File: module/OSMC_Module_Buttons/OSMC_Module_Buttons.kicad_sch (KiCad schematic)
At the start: 4 parts, among them J1 Conn_01x08_Socket, U1 OSMC Module Board w/pins, U2 24LC02BT-I/OT, U3 PCF8574DWR

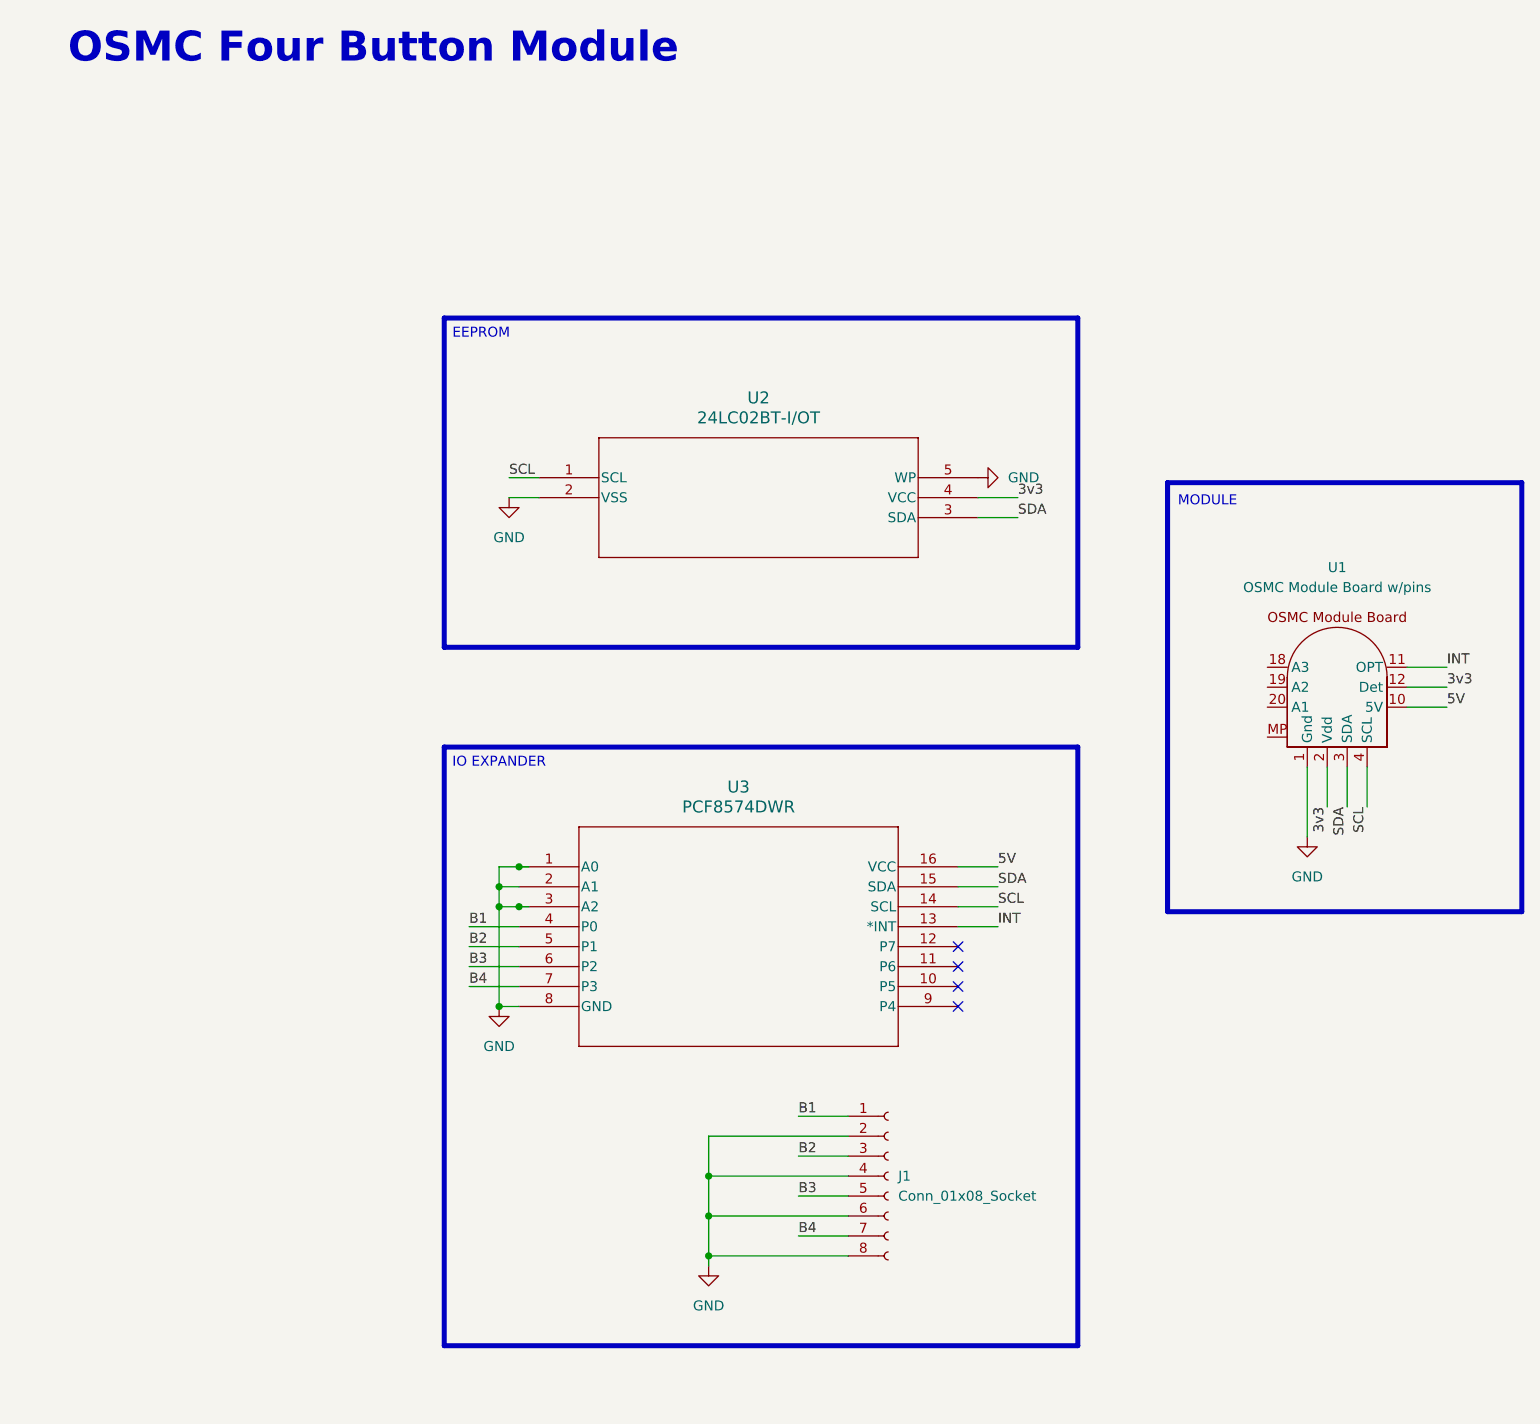
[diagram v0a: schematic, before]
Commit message: cleared via and traces
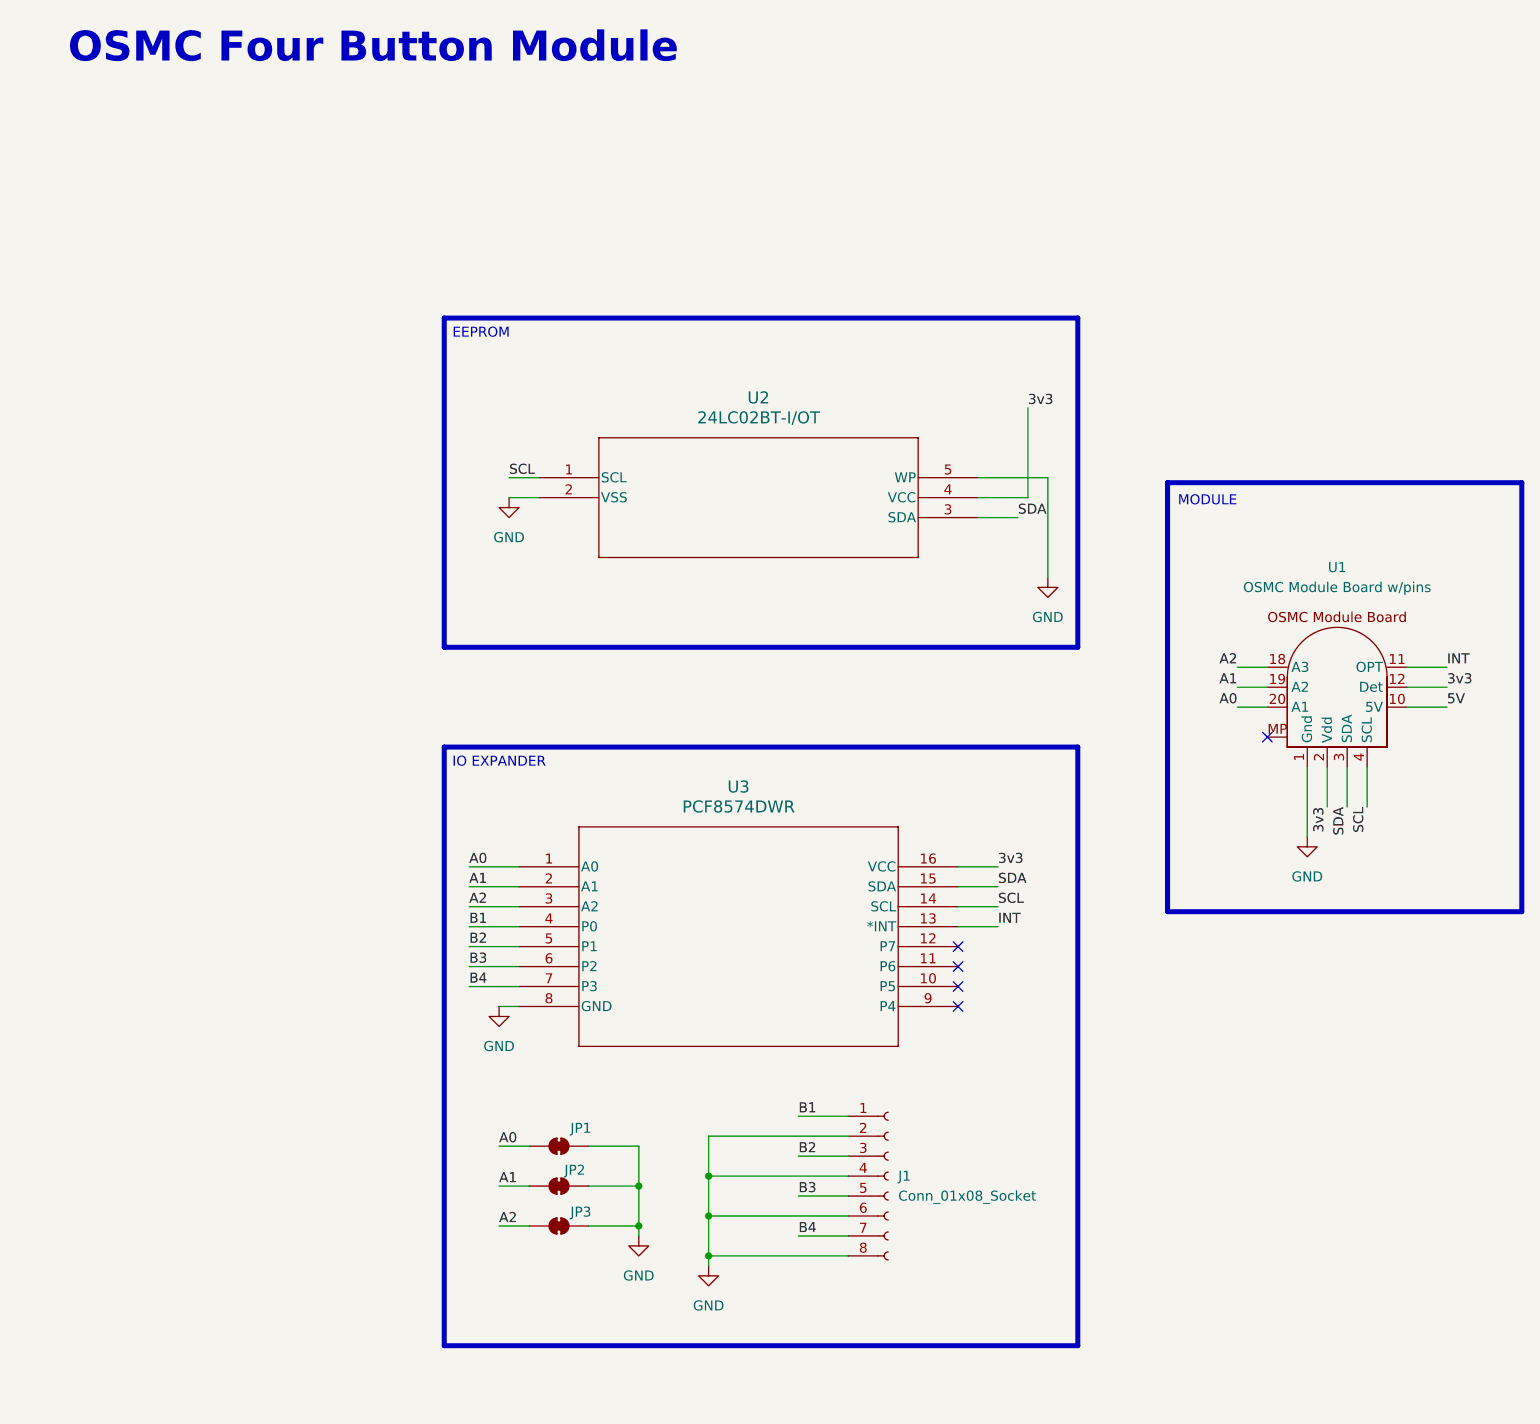
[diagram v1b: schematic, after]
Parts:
- added JP1, JP2, JP3: SolderJumper_2_Bridged, Jumper:SolderJumper-2_P1.3mm_Bridged2Bar_Pad1.0x1.5mm, symbol Jumper:SolderJumper_2_Bridged
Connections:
- net 3v3: now also U3.16 (VCC)
- net 5V: no longer U3.16 (VCC)
- net GND: now also JP1.2 (B), JP2.2 (B), JP3.2 (B); no longer U3.1 (A0), U3.2 (A1), U3.3 (A2)
- net A2: now reaches U1.18 (A3)
- net A2: now also U3.3 (A2), JP3.1 (A)
- net A1: now reaches U1.19 (A2)
- net A1: now also U3.2 (A1), JP2.1 (A)
- net A0: now reaches U1.20 (A1)
- net A0: now also U3.1 (A0), JP1.1 (A)
- no-connect marks 4 -> 5

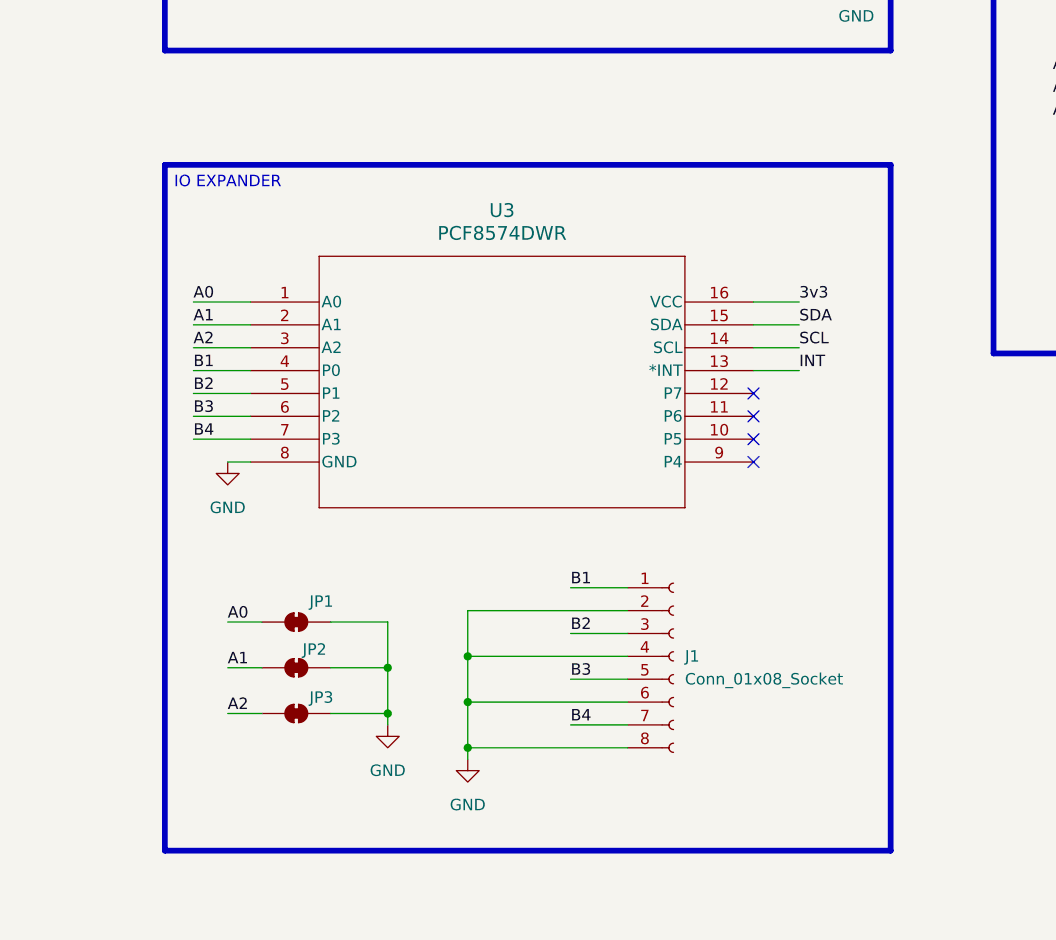
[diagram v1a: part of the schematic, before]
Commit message: update to modules gerbers produced
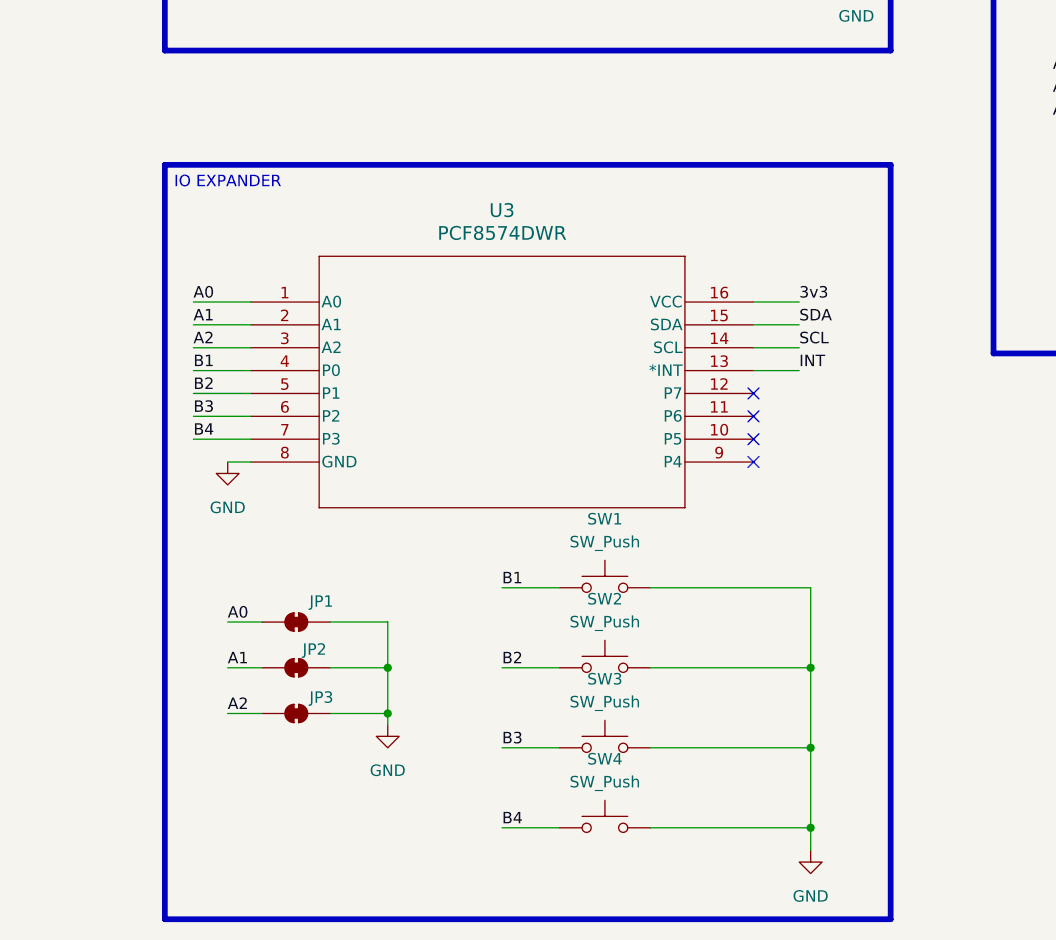
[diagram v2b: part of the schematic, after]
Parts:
- removed J1: Conn_01x08_Socket, Library:OSMC_Button_Membrane, symbol Library:Conn_01x08_Socket
- added SW1, SW2, SW3, SW4: SW_Push, footprints:SW_Push_1P1T_XKB_TS-1187A, symbol Switch:SW_Push
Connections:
- net B1: now also SW1.1
- net B2: now also SW2.1
- net B3: now also SW3.1
- net B4: now also SW4.1
- net GND: now also SW1.2, SW2.2, SW3.2, SW4.2

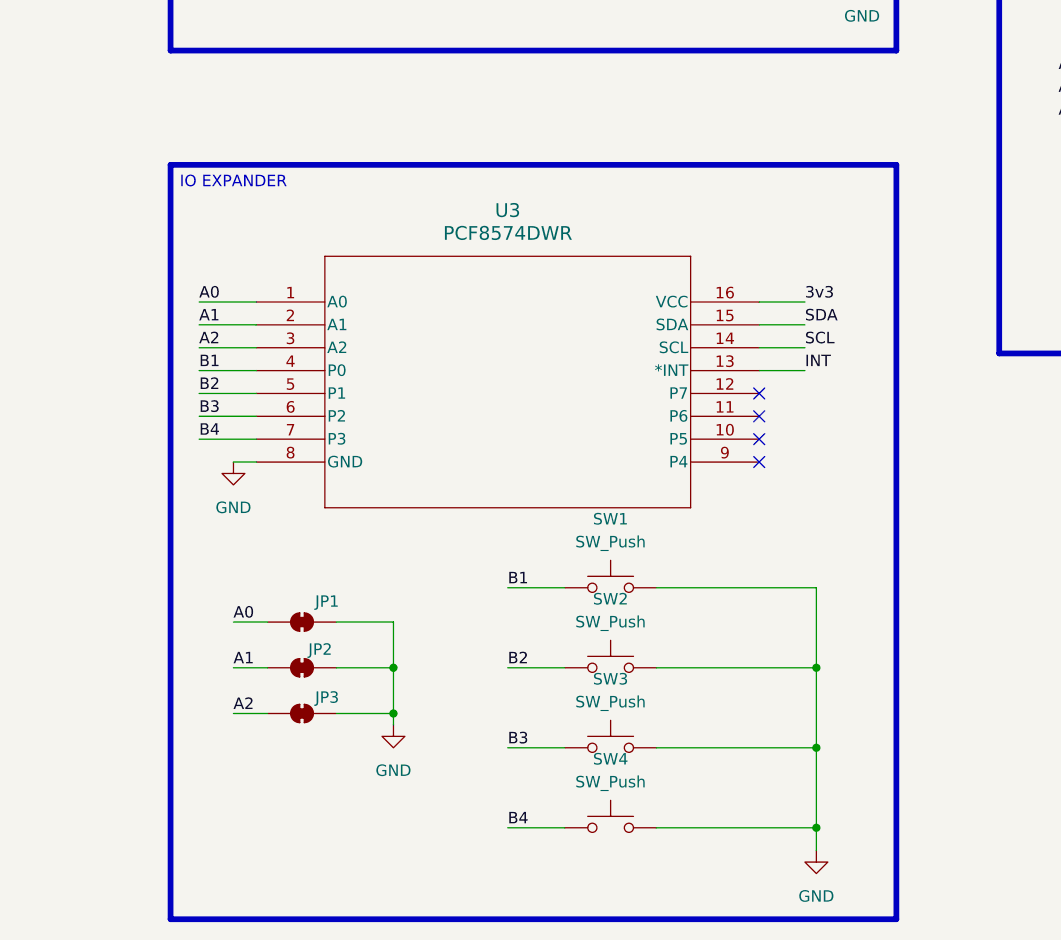
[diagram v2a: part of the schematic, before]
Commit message: fixed diode direction
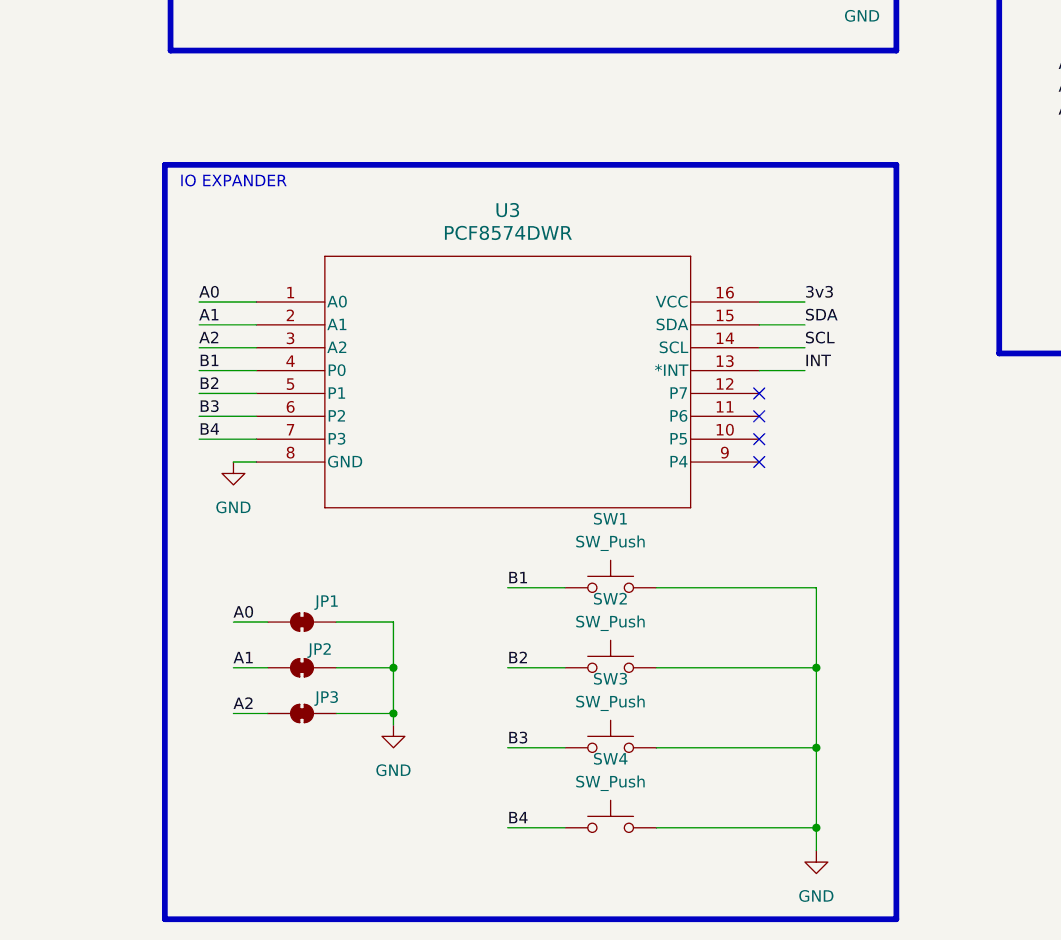
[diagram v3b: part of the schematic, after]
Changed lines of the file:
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@@
 	)
 	(rectangle
-		(start 61.595 107.95)
+		(start 60.96 107.95)
 		(end 142.24 191.77)
 		(stroke
@@
 	)
 	(no_connect
-		(at 127 140.97)
+		(at 127 138.43)
 	)
 	(no_connect
@@
 	)
 	(no_connect
-		(at 127 138.43)
+		(at 127 140.97)
 	)
 	(no_connect
